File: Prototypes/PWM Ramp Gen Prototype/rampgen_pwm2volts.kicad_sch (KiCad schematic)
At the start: 8 parts, among them U8 74LVC1G97

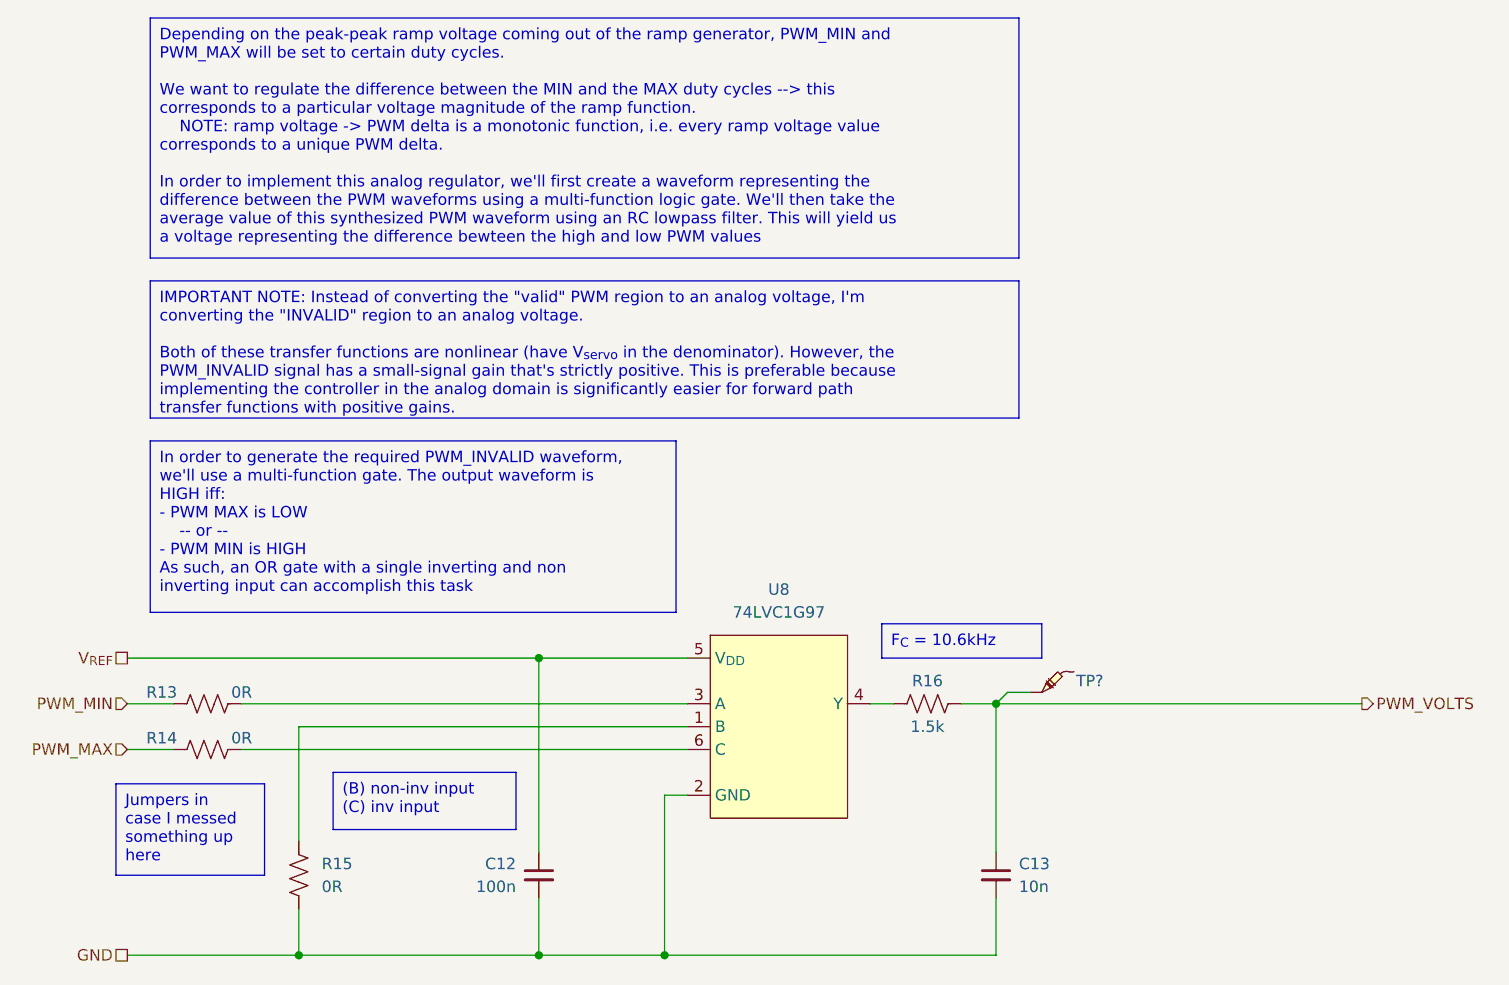
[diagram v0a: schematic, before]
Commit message: Comparator and Op-amp tweaks for BOM consolidation; final layout
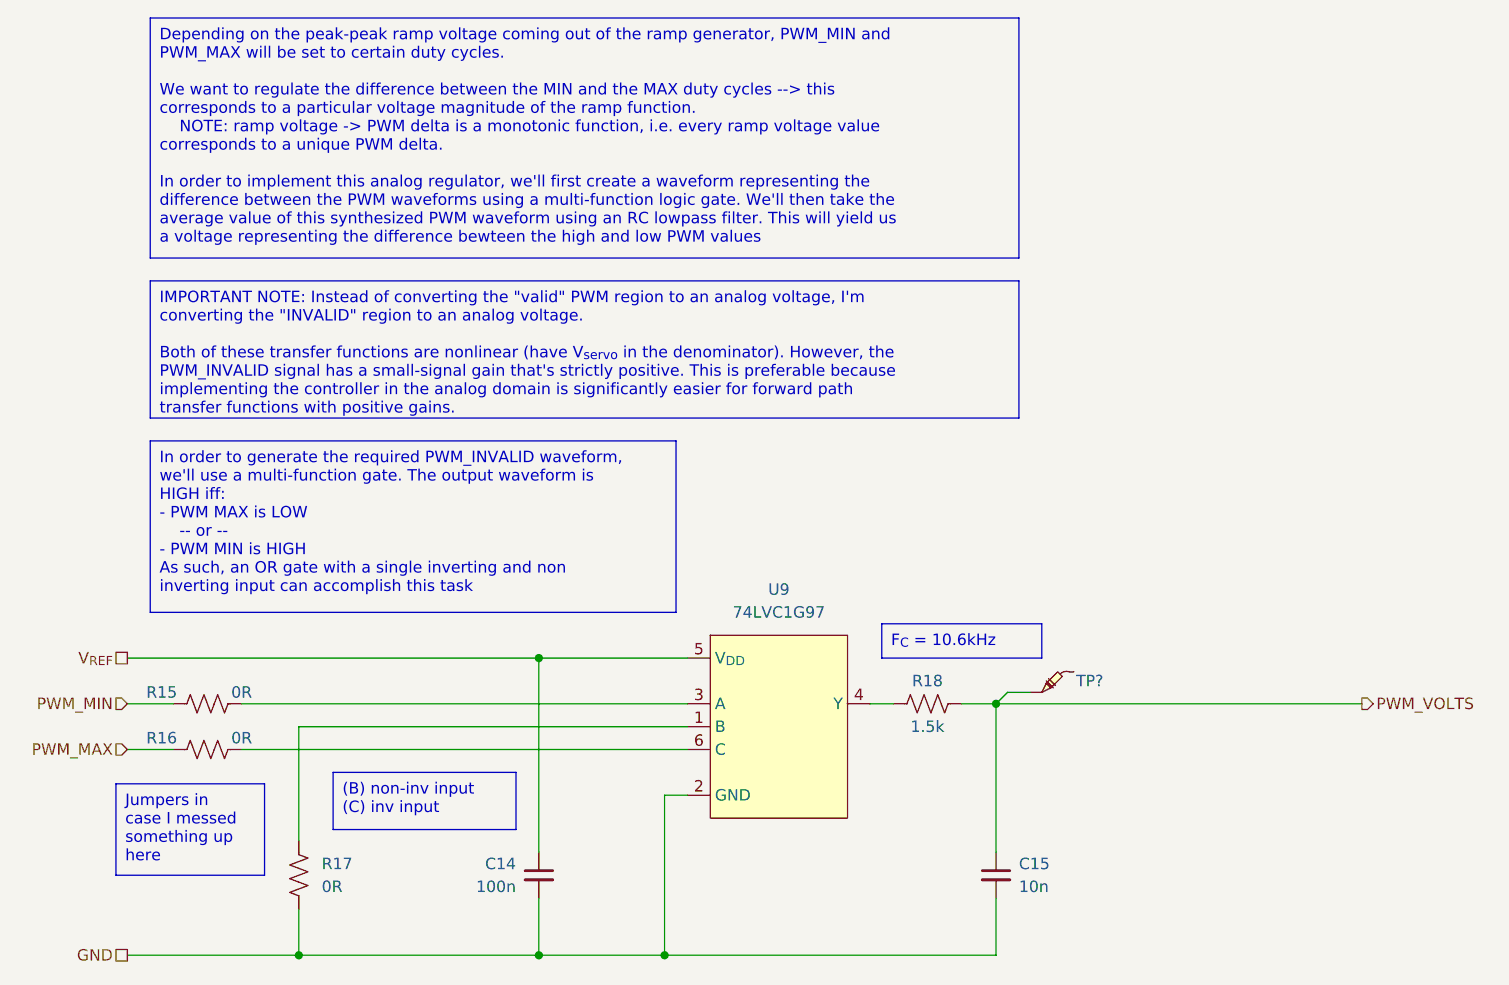
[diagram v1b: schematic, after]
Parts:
- renumbered C12 to C14, C13 to C15, R13 to R15, R14 to R16, R15 to R17, R16 to R18, U8 to U9
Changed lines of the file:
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@@
   (symbol (lib_id "Custom-Resistor:RMCF0603FT1K50") (at 175.26 101.6 90) (unit 1)
     (in_bom yes) (on_board yes) (dnp no)
-    (property "Reference" "R16" (at 175.26 99.06 90)
+    (property "Reference" "R18" (at 175.26 99.06 90)
       (effects (font (size 1.27 1.27)))
     )
@@
       (project "PWM Ramp Gen Prototype"
         (path "/a1dfcc81-abac-4d0f-af30-e0b6fd53034d/96805dea-d843-4551-a066-0332d83937cc"
+          (reference "R18") (unit 1)
+        )
+      )
+    )
+  )
+  (symbol (lib_id "Custom-Resistor:RMCF0603ZT0R00") (at 95.25 106.68 90) (unit 1)
+    (in_bom yes) (on_board yes) (dnp no)
+    (property "Reference" "R16" (at 90.17 105.41 90)
+      (effects (font (size 1.27 1.27)))
+    )
+    (property "Value" "0R" (at 99.06 105.41 90)
+      (effects (font (size 1.27 1.27)))
+    )
+    (property "Footprint" "Resistor_SMD:R_0603_1608Metric_Pad0.98x0.95mm_HandSolder" (at 95.504 105.664 90)
+      (effects (font (size 1.27 1.27)) hide)
+    )
+    (property "Datasheet" "https://www.seielect.com/Catalog/SEI-RMCF_RMCP.pdf" (at 95.25 106.68 0)
+      (effects (font (size 1.27 1.27)) hide)
+    )
+    (property "Manufacturer" "Stackpole Electronics Inc" (at 95.25 106.68 0)
+      (effects (font (size 1.27 1.27)) hide)
+    )
+    (property "Part Number" "RMCF0603ZT0R00" (at 95.25 106.68 0)
+      (effects (font (size 1.27 1.27)) hide)
+    )
+    (pin "1")
+    (pin "2")
+    (instances
+      (project "PWM Ramp Gen Prototype"
+        (path "/a1dfcc81-abac-4d0f-af30-e0b6fd53034d/96805dea-d843-4551-a066-0332d83937cc"
           (reference "R16") (unit 1)
         )
@@
     )
   )
-  (symbol (lib_id "Custom-Resistor:RMCF0603ZT0R00") (at 95.25 106.68 90) (unit 1)
-    (in_bom yes) (on_board yes) (dnp no)
-    (property "Reference" "R14" (at 90.17 105.41 90)
-      (effects (font (size 1.27 1.27)))
-    )
-    (property "Value" "0R" (at 99.06 105.41 90)
-      (effects (font (size 1.27 1.27)))
-    )
-    (property "Footprint" "Resistor_SMD:R_0603_1608Metric_Pad0.98x0.95mm_HandSolder" (at 95.504 105.664 90)
-      (effects (font (size 1.27 1.27)) hide)
-    )
-    (property "Datasheet" "https://www.seielect.com/Catalog/SEI-RMCF_RMCP.pdf" (at 95.25 106.68 0)
-      (effects (font (size 1.27 1.27)) hide)
-    )
-    (property "Manufacturer" "Stackpole Electronics Inc" (at 95.25 106.68 0)
-      (effects (font (size 1.27 1.27)) hide)
-    )
-    (property "Part Number" "RMCF0603ZT0R00" (at 95.25 106.68 0)
-      (effects (font (size 1.27 1.27)) hide)
-    )
-    (pin "1")
-    (pin "2")
-    (instances
-      (project "PWM Ramp Gen Prototype"
-        (path "/a1dfcc81-abac-4d0f-af30-e0b6fd53034d/96805dea-d843-4551-a066-0332d83937cc"
-          (reference "R14") (unit 1)
-        )
-      )
-    )
-  )
   (symbol (lib_id "Custom-Resistor:RMCF0603ZT0R00") (at 95.25 101.6 90) (unit 1)
     (in_bom yes) (on_board yes) (dnp no)
-    (property "Reference" "R13" (at 90.17 100.33 90)
+    (property "Reference" "R15" (at 90.17 100.33 90)
       (effects (font (size 1.27 1.27)))
     )
@@
       (project "PWM Ramp Gen Prototype"
         (path "/a1dfcc81-abac-4d0f-af30-e0b6fd53034d/96805dea-d843-4551-a066-0332d83937cc"
-          (reference "R13") (unit 1)
+          (reference "R15") (unit 1)
         )
       )
@@
   (symbol (lib_id "Custom-LogicIC:1G97") (at 158.75 104.14 0) (unit 1)
     (in_bom yes) (on_board yes) (dnp no) (fields_autoplaced)
-    (property "Reference" "U8" (at 158.75 88.9 0)
+    (property "Reference" "U9" (at 158.75 88.9 0)
       (effects (font (size 1.27 1.27)))
     )
@@
       (project "PWM Ramp Gen Prototype"
         (path "/a1dfcc81-abac-4d0f-af30-e0b6fd53034d/96805dea-d843-4551-a066-0332d83937cc"
-          (reference "U8") (unit 1)
+          (reference "U9") (unit 1)
         )
       )
@@
         )
         (path "/a1dfcc81-abac-4d0f-af30-e0b6fd53034d/96805dea-d843-4551-a066-0332d83937cc"
-          (reference "TP23") (unit 1)
+          (reference "TP21") (unit 1)
         )
       )
@@
   (symbol (lib_id "Custom-Capacitor:CL10B104KB8NNWC") (at 132.08 120.65 0) (mirror y) (unit 1)
     (in_bom yes) (on_board yes) (dnp no)
-    (property "Reference" "C12" (at 129.54 119.3863 0)
+    (property "Reference" "C14" (at 129.54 119.3863 0)
       (effects (font (size 1.27 1.27)) (justify left))
     )
@@
       (project "PWM Ramp Gen Prototype"
         (path "/a1dfcc81-abac-4d0f-af30-e0b6fd53034d/96805dea-d843-4551-a066-0332d83937cc"
-          (reference "C12") (unit 1)
+          (reference "C14") (unit 1)
         )
       )
@@
   (symbol (lib_id "Custom-Resistor:RMCF0603ZT0R00") (at 105.41 120.65 0) (unit 1)
     (in_bom yes) (on_board yes) (dnp no) (fields_autoplaced)
-    (property "Reference" "R15" (at 107.95 119.38 0)
+    (property "Reference" "R17" (at 107.95 119.38 0)
       (effects (font (size 1.27 1.27)) (justify left))
     )
@@
       (project "PWM Ramp Gen Prototype"
         (path "/a1dfcc81-abac-4d0f-af30-e0b6fd53034d/96805dea-d843-4551-a066-0332d83937cc"
-          (reference "R15") (unit 1)
+          (reference "R17") (unit 1)
         )
       )
@@
   (symbol (lib_id "Custom-Capacitor:CL10B103KB8NNNC") (at 182.88 120.65 0) (unit 1)
     (in_bom yes) (on_board yes) (dnp no) (fields_autoplaced)
-    (property "Reference" "C13" (at 185.42 119.3863 0)
+    (property "Reference" "C15" (at 185.42 119.3863 0)
       (effects (font (size 1.27 1.27)) (justify left))
     )
@@
       (project "PWM Ramp Gen Prototype"
         (path "/a1dfcc81-abac-4d0f-af30-e0b6fd53034d/96805dea-d843-4551-a066-0332d83937cc"
-          (reference "C13") (unit 1)
-        )
-      )
+          (reference "C15") (unit 1)
+        )
+      )
